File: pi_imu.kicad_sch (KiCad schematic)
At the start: 13 parts, among them J10 BM04B-GHS-TBT, J11 BM04B-GHS-TBT, J12 Conn_01x05_Pin, J13 Conn_01x03_Pin, J14 Conn_01x03_Pin, J9 Conn_01x04_Pin, U1 4754, U10 4754, U8 RASPBERRY_PI_4B_4GB

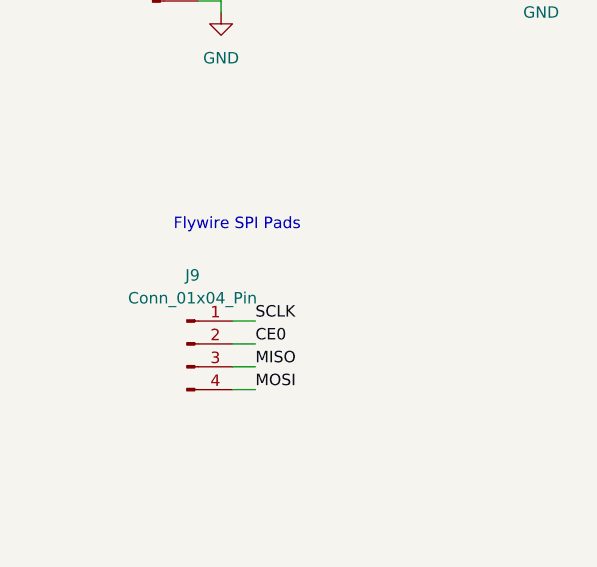
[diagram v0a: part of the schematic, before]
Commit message: Added header and updated mounting pins
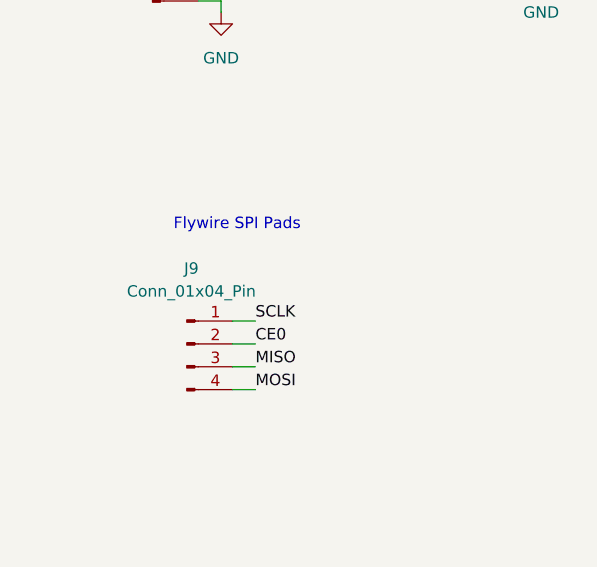
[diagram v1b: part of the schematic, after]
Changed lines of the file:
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@@
 		(on_board yes)
 		(dnp no)
-		(fields_autoplaced yes)
 		(property "Reference" "J9"
-			(at 41.275 77.47 0)
+			(at 41.148 76.708 0)
 			(effects
 				(font
@@
 		)
 		(property "Value" "Conn_01x04_Pin"
-			(at 41.275 80.01 0)
+			(at 41.148 79.248 0)
 			(effects
 				(font

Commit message: Initial Component Placement
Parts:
- U8: footprint RASPBERRY_PI_4B_4GB:MODULE_RASPBERRY_PI_4B_4GB -> TSW-120-09-G-D:SAMTEC_TSW-120-09-G-D
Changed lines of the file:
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@@
 			)
 		)
-		(property "Footprint" "RASPBERRY_PI_4B_4GB:MODULE_RASPBERRY_PI_4B_4GB"
+		(property "Footprint" "TSW-120-09-G-D:SAMTEC_TSW-120-09-G-D"
 			(at 149.86 102.87 0)
 			(effects

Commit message: Routing
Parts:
- removed J14: Conn_01x03_Pin, Connector_PinHeader_2.54mm:PinHeader_1x03_P2.54mm_Vertical, symbol Connector:Conn_01x03_Pin
- removed J9: Conn_01x04_Pin, Connector_PinHeader_2.54mm:PinHeader_1x04_P2.54mm_Vertical, symbol Connector:Conn_01x04_Pin
- J13: footprint Connector_PinHeader_2.54mm:PinHeader_1x05_P2.54mm_Vertical -> Connector_PinHeader_2.54mm:PinHeader_1x03_P2.54mm_Vertical
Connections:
- net GND: now also J13.1 (Pin_1); no longer J13.3 (Pin_3)
- net SCL: now also J13.3 (Pin_3); no longer J13.2 (Pin_2)
- net SDA: now also J13.2 (Pin_2); no longer J13.1 (Pin_1)
- no-connect marks 23 -> 16
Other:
- note removed: "Flywire SPI Pads"
- note removed: "UART Connector"

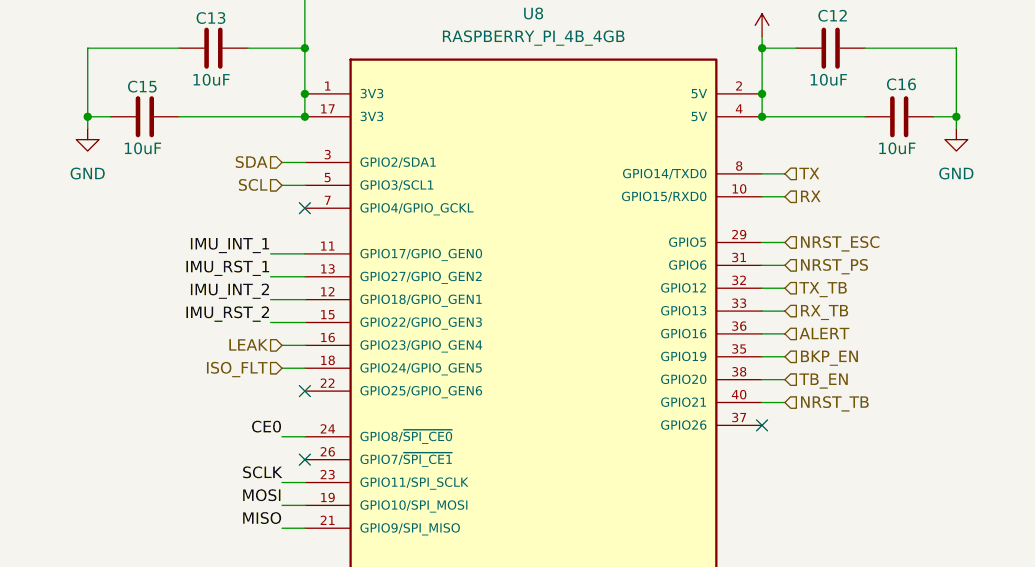
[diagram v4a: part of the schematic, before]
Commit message: Finished Routing
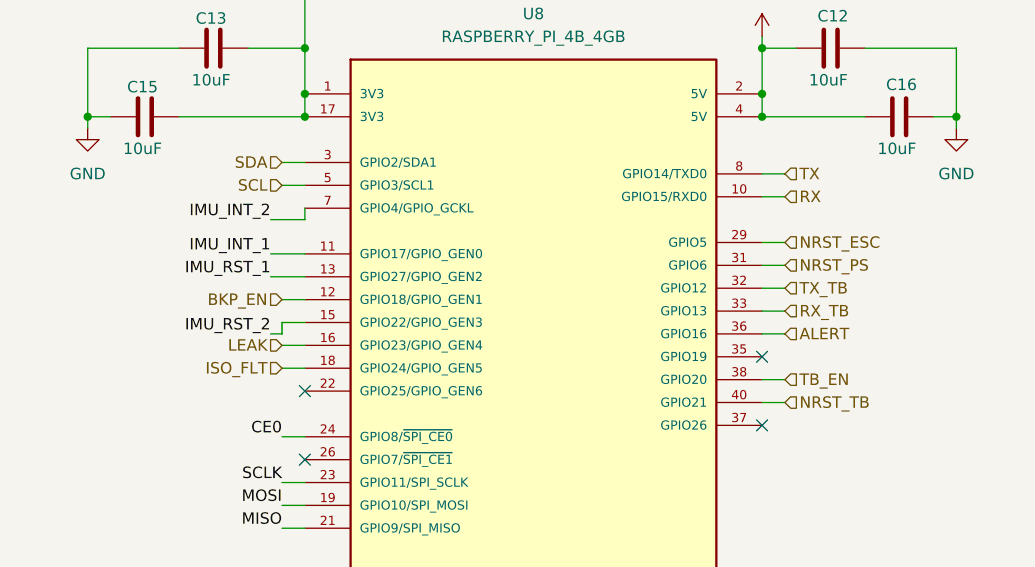
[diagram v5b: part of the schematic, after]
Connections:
- net BKP_EN: now also U8.12 (GPIO18/GPIO_GEN1); no longer U8.35 (GPIO19)
- net IMU_INT_2: now also U8.7 (GPIO4/GPIO_GCKL); no longer U8.12 (GPIO18/GPIO_GEN1)
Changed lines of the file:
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@@
+	)
+	(no_connect
+		(at 175.26 102.87)
 	)
 	(no_connect
@@
 	)
 	(no_connect
-		(at 124.46 86.36)
-	)
-	(no_connect
 		(at 228.6 113.03)
 	)
@@
 	(wire
 		(pts
+			(xy 121.92 100.33) (xy 121.92 99.06)
+		)
+		(stroke
+			(width 0)
+			(type default)
+		)
+	)
+	(wire
+		(pts
 			(xy 27.94 143.51) (xy 30.48 143.51)
 		)
@@
 	(wire
 		(pts
-			(xy 175.26 102.87) (xy 177.8 102.87)
+			(xy 124.46 96.52) (xy 121.92 96.52)
 		)
 		(stroke
@@
 	(wire
 		(pts
-			(xy 124.46 99.06) (xy 120.65 99.06)
+			(xy 121.92 100.33) (xy 120.65 100.33)
 		)
 		(stroke
@@
 	(wire
 		(pts
+			(xy 124.46 87.63) (xy 120.65 87.63)
+		)
+		(stroke
+			(width 0)
+			(type default)
+		)
+	)
+	(wire
+		(pts
 			(xy 194.31 76.2) (xy 196.85 76.2)
 		)
@@
 	(wire
 		(pts
+			(xy 121.92 99.06) (xy 124.46 99.06)
+		)
+		(stroke
+			(width 0)
+			(type default)
+		)
+	)
+	(wire
+		(pts
 			(xy 27.94 138.43) (xy 30.48 138.43)
 		)
@@
 	(wire
 		(pts
+			(xy 124.46 87.63) (xy 124.46 86.36)
+		)
+		(stroke
+			(width 0)
+			(type default)
+		)
+	)
+	(wire
+		(pts
 			(xy 27.94 146.05) (xy 30.48 146.05)
-		)
-		(stroke
-			(width 0)
-			(type default)
-		)
-	)
-	(wire
-		(pts
-			(xy 124.46 96.52) (xy 120.65 96.52)
 		)
 		(stroke
@@
 		)
 	)
+	(label "IMU_INT_2"
+		(at 120.65 87.63 180)
+		(fields_autoplaced yes)
+		(effects
+			(font
+				(size 1.27 1.27)
+			)
+			(justify right bottom)
+		)
+	)
 	(label "SCLK"
 		(at 121.92 116.84 180)
@@
 		)
 	)
-	(label "IMU_INT_2"
-		(at 120.65 96.52 180)
-		(fields_autoplaced yes)
-		(effects
-			(font
-				(size 1.27 1.27)
-			)
-			(justify right bottom)
-		)
-	)
 	(label "IMU_RST_1"
 		(at 120.65 93.98 180)
@@
 	)
 	(label "IMU_RST_2"
-		(at 120.65 99.06 180)
+		(at 120.65 100.33 180)
 		(fields_autoplaced yes)
 		(effects
@@
 		)
 	)
+	(hierarchical_label "BKP_EN"
+		(shape input)
+		(at 121.92 96.52 180)
+		(fields_autoplaced yes)
+		(effects
+			(font
+				(size 1.27 1.27)
+			)
+			(justify right)
+		)
+	)
 	(hierarchical_label "RX_TB"
 		(shape input)
@@
 		)
 	)
-	(hierarchical_label "BKP_EN"
-		(shape input)
-		(at 177.8 102.87 0)
-		(fields_autoplaced yes)
-		(effects
-			(font
-				(size 1.27 1.27)
-			)
-			(justify left)
-		)
-	)

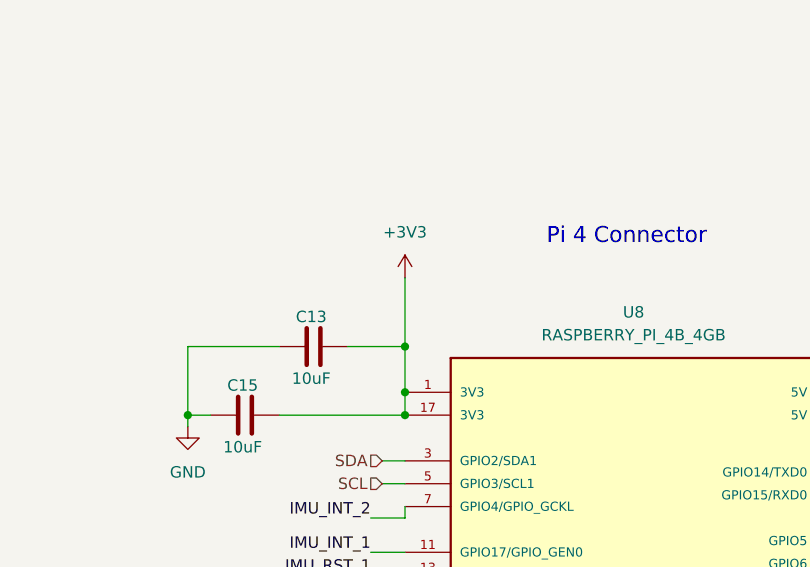
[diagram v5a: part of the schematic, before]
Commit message: fixed several DRC errors and ferrite bead package size, still reviewing the board
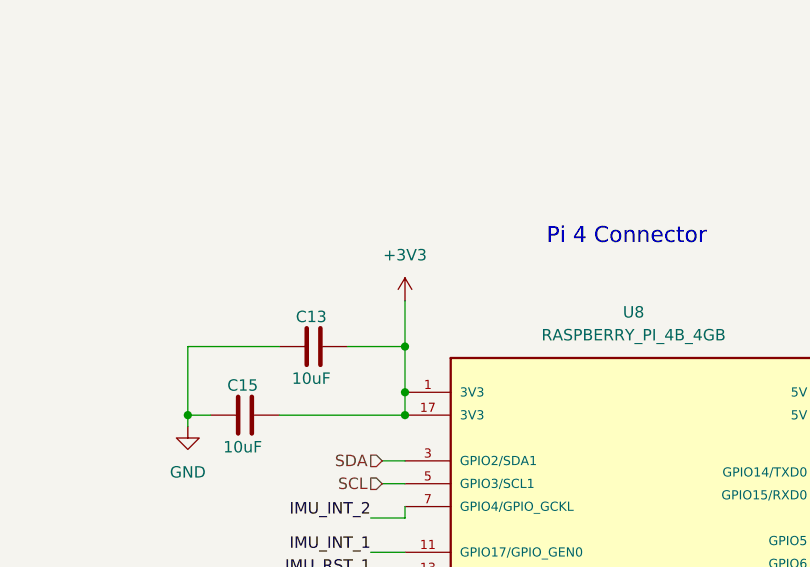
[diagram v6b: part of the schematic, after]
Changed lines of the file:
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@@
 	(paper "A4")
 	(junction
-		(at 124.46 73.66)
+		(at 175.26 73.66)
 		(diameter 0)
 		(color 0 0 0 0)
 	)
 	(junction
-		(at 175.26 73.66)
+		(at 175.26 68.58)
 		(diameter 0)
 		(color 0 0 0 0)
 	)
 	(junction
-		(at 175.26 68.58)
+		(at 124.46 76.2)
 		(diameter 0)
 		(color 0 0 0 0)
@@
 	)
 	(junction
-		(at 124.46 76.2)
+		(at 124.46 73.66)
 		(diameter 0)
 		(color 0 0 0 0)
@@
 	(wire
 		(pts
+			(xy 124.46 68.58) (xy 124.46 73.66)
+		)
+		(stroke
+			(width 0)
+			(type default)
+		)
+	)
+	(wire
+		(pts
 			(xy 260.35 81.28) (xy 260.35 85.09)
 		)
@@
 	(wire
 		(pts
-			(xy 124.46 68.58) (xy 124.46 73.66)
-		)
-		(stroke
-			(width 0)
-			(type default)
-		)
-	)
-	(wire
-		(pts
 			(xy 257.81 81.28) (xy 260.35 81.28)
 		)
@@
 	(wire
 		(pts
-			(xy 124.46 60.96) (xy 124.46 68.58)
+			(xy 124.46 63.5) (xy 124.46 68.58)
 		)
 		(stroke
@@
 	(wire
 		(pts
-			(xy 124.46 73.66) (xy 124.46 76.2)
-		)
-		(stroke
-			(width 0)
-			(type default)
-		)
-	)
-	(wire
-		(pts
 			(xy 100.33 76.2) (xy 100.33 77.47)
 		)
@@
 	(wire
 		(pts
+			(xy 124.46 73.66) (xy 124.46 76.2)
+		)
+		(stroke
+			(width 0)
+			(type default)
+		)
+	)
+	(wire
+		(pts
 			(xy 224.79 55.88) (xy 227.33 55.88)
 		)
@@
 	(symbol
 		(lib_id "power:+3V3")
-		(at 124.46 60.96 0)
+		(at 124.46 63.5 0)
 		(unit 1)
 		(exclude_from_sim no)
@@
 		(fields_autoplaced yes)
 		(property "Reference" "#PWR012"
-			(at 124.46 64.77 0)
+			(at 124.46 67.31 0)
 			(effects
 				(font
@@
 		)
 		(property "Value" "+3V3"
-			(at 124.46 55.88 0)
+			(at 124.46 58.42 0)
 			(effects
 				(font
@@
 		)
 		(property "Footprint" ""
-			(at 124.46 60.96 0)
+			(at 124.46 63.5 0)
 			(effects
 				(font
@@
 		)
 		(property "Datasheet" ""
-			(at 124.46 60.96 0)
+			(at 124.46 63.5 0)
 			(effects
 				(font
@@
 		)
 		(property "Description" "Power symbol creates a global label with name \"+3V3\""
-			(at 124.46 60.96 0)
+			(at 124.46 63.5 0)
 			(effects
 				(font
